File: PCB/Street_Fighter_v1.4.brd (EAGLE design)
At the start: 59.9 x 77.5 mm, 76 parts, among them J1 FEMALE 2x3, Q1 BSS138, Q10 BSS138, Q2 BSS138, Q3 FQP30N06L, Q4 BSS138, Q5 BSS138, Q6 BSS138, Q7 BSS138, Q9 BSS138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

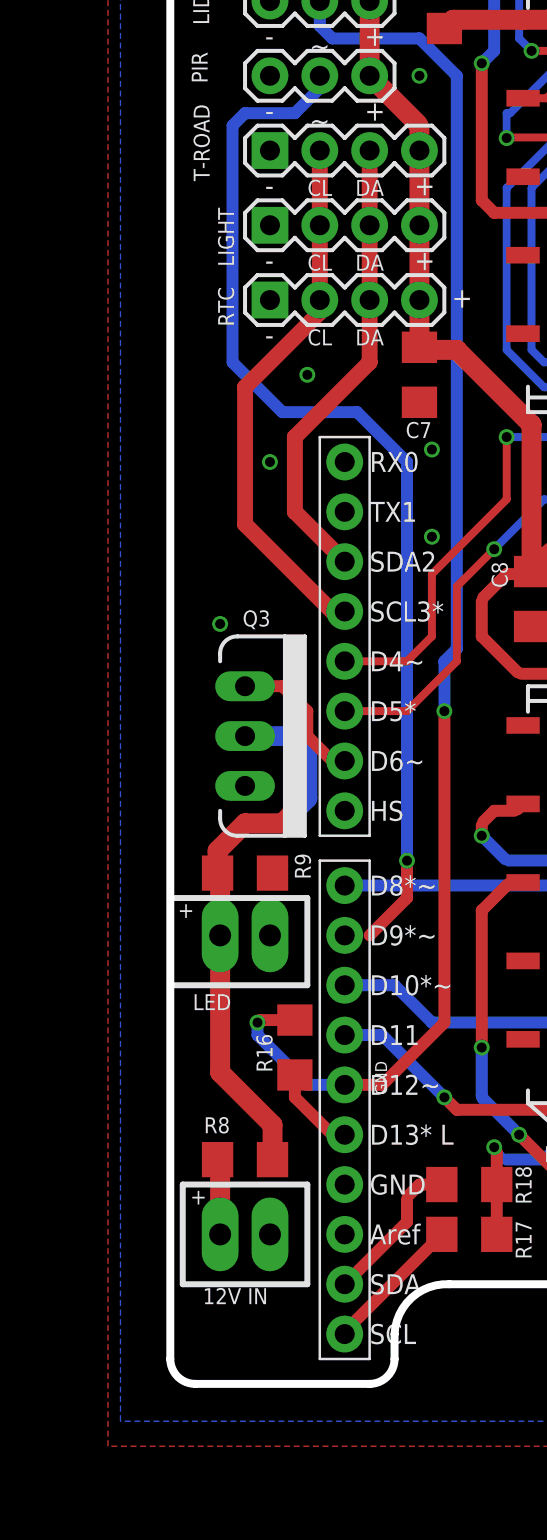
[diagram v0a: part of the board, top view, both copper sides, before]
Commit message: Updated mounting plate for traffic sensors. Also started adding in the possibility for more than 2 PIR sensors.
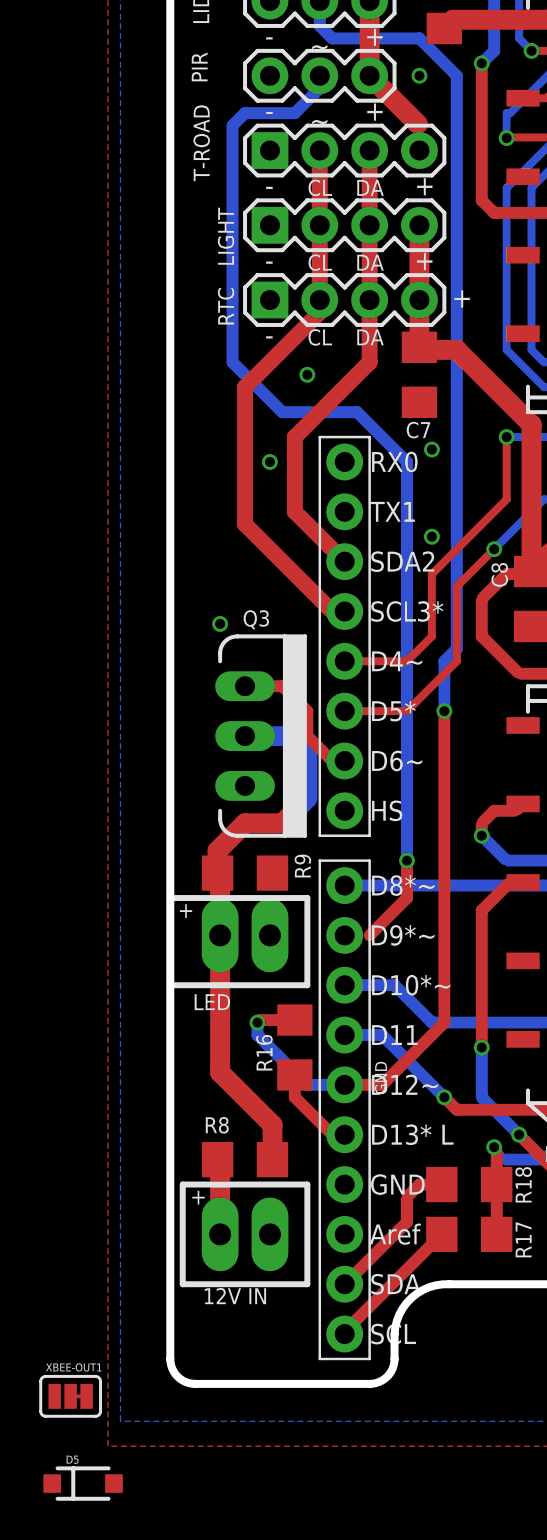
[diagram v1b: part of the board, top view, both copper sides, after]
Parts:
- added D5: 1N4148W, SparkFun-DiscreteSemi:SOD-123
- added XBEE-OUT1: JUMPER-PAD-3-2OF3_NC_BY_TRACE_SMALL, SparkFun-Passives:PAD-JUMPER-3-2OF3_NC_BY_TRACE_YES_SILK_FULL_BOX
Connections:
- new net N$7: D5.C, XBEE-OUT1.3
- new net N$8: T-ROAD.4, XBEE-OUT1.2
- net +3V3: now also D5.A
- net +5V: now also XBEE-OUT1.1; no longer T-ROAD.4
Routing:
- net +5V: track 233.0 -> 228.0 mm
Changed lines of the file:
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@@
 <element name="R31" library="SparkFun-Passives" package="1206" value="4.7K" x="52.07" y="11.43" rot="R180"/>
 <element name="R32" library="SparkFun-Passives" package="1206" value="4.7K" x="43.18" y="38.1" rot="R270"/>
+<element name="XBEE-OUT1" library="SparkFun-Passives" package="PAD-JUMPER-3-2OF3_NC_BY_TRACE_YES_SILK_FULL_BOX" value="JUMPER-PAD-3-2OF3_NC_BY_TRACE_SMALL" x="-5.08" y="-0.635"/>
+<element name="D5" library="SparkFun-DiscreteSemi" package="SOD-123" value="1N4148W" x="-4.445" y="-5.08"/>
 </elements>
 <signals>
@@
 <contactref element="SOUND" pad="3"/>
 <contactref element="PIR" pad="3"/>
-<contactref element="T-ROAD" pad="4"/>
 <contactref element="C7" pad="2"/>
 <contactref element="R18" pad="2"/>
@@
 <wire x1="10.16" y1="73.424790625" x2="10.23439375" y2="73.60439375" width="1.016" layer="1" curve="-44.999502"/>
 <wire x1="10.23439375" y1="73.60439375" x2="10.29" y2="73.66" width="0.3048" layer="1"/>
-<wire x1="12.7" y1="62.865" x2="12.7" y2="64.029790625" width="1.016" layer="1"/>
 <wire x1="12.7" y1="64.029790625" x2="12.62560625" y2="64.20939375" width="0.3048" layer="1" curve="44.999502"/>
 <wire x1="12.62560625" y1="64.20939375" x2="10.16" y2="66.675" width="1.016" layer="1"/>
-<wire x1="12.7" y1="59.055" x2="12.7" y2="62.865" width="1.016" layer="1"/>
 <wire x1="12.7" y1="59.055" x2="12.7" y2="55.245" width="1.016" layer="1"/>
 <wire x1="12.7" y1="55.245" x2="12.7" y2="52.940209375" width="0.3048" layer="1"/>
@@
 <wire x1="48.26" y1="8.89" x2="50.67" y2="11.3" width="0.6096" layer="1"/>
 <wire x1="50.67" y1="11.3" x2="50.67" y2="11.43" width="0.6096" layer="1"/>
+<contactref element="XBEE-OUT1" pad="1"/>
+<wire x1="12.7" y1="59.055" x2="12.7" y2="64.029790625" width="0" layer="19" extent="1-1"/>
+<wire x1="-5.8928" y1="-0.635" x2="16.64" y2="7.62" width="0" layer="19" extent="1-1"/>
 </signal>
 <signal name="+3V3">
@@
 <wire x1="30.48" y1="71.12" x2="31.75" y2="71.12" width="1.016" layer="1"/>
 <wire x1="36.96" y1="55.115" x2="37.465" y2="54.61" width="1.016" layer="1"/>
+<contactref element="D5" pad="A"/>
+<wire x1="-2.87" y1="-5.08" x2="31.58" y2="14.29" width="0" layer="19" extent="1-1"/>
 </signal>
 <signal name="V+">
@@
 <wire x1="8.89" y1="22.86" x2="10.16" y2="22.86" width="0" layer="19" extent="1-1"/>
 </signal>
+<signal name="N$8">
+<contactref element="T-ROAD" pad="4"/>
+<contactref element="XBEE-OUT1" pad="2"/>
+<wire x1="-4.445" y1="-0.635" x2="12.7" y2="62.865" width="0" layer="19" extent="1-1"/>
+</signal>
+<signal name="N$7">
+<contactref element="XBEE-OUT1" pad="3"/>
+<contactref element="D5" pad="C"/>
+<wire x1="-4.2672" y1="-0.635" x2="-6.02" y2="-5.08" width="0" layer="19" extent="1-1"/>
+</signal>
 </signals>
